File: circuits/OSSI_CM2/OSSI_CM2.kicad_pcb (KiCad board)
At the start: 4 copper layers, 49.5 x 54.9 mm, 76 parts, among them U101 STM32L412C8T6, U103 LM75B, U104 OPA2317, X101 PINHEADER_2×5, X201 Conn_01x20_Pin, X202 Conn_01x21_Pin, Y101 10MHz

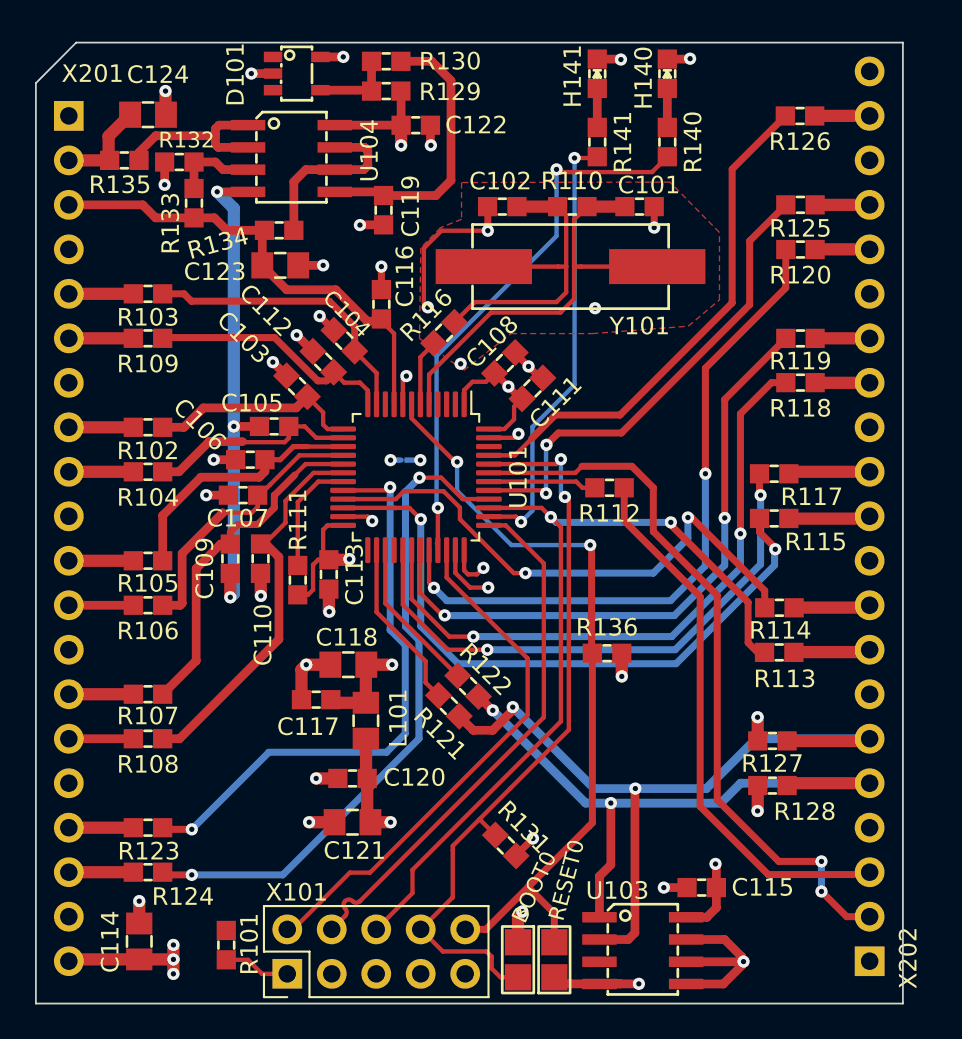
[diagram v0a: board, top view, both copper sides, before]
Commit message: Updates footprint paths
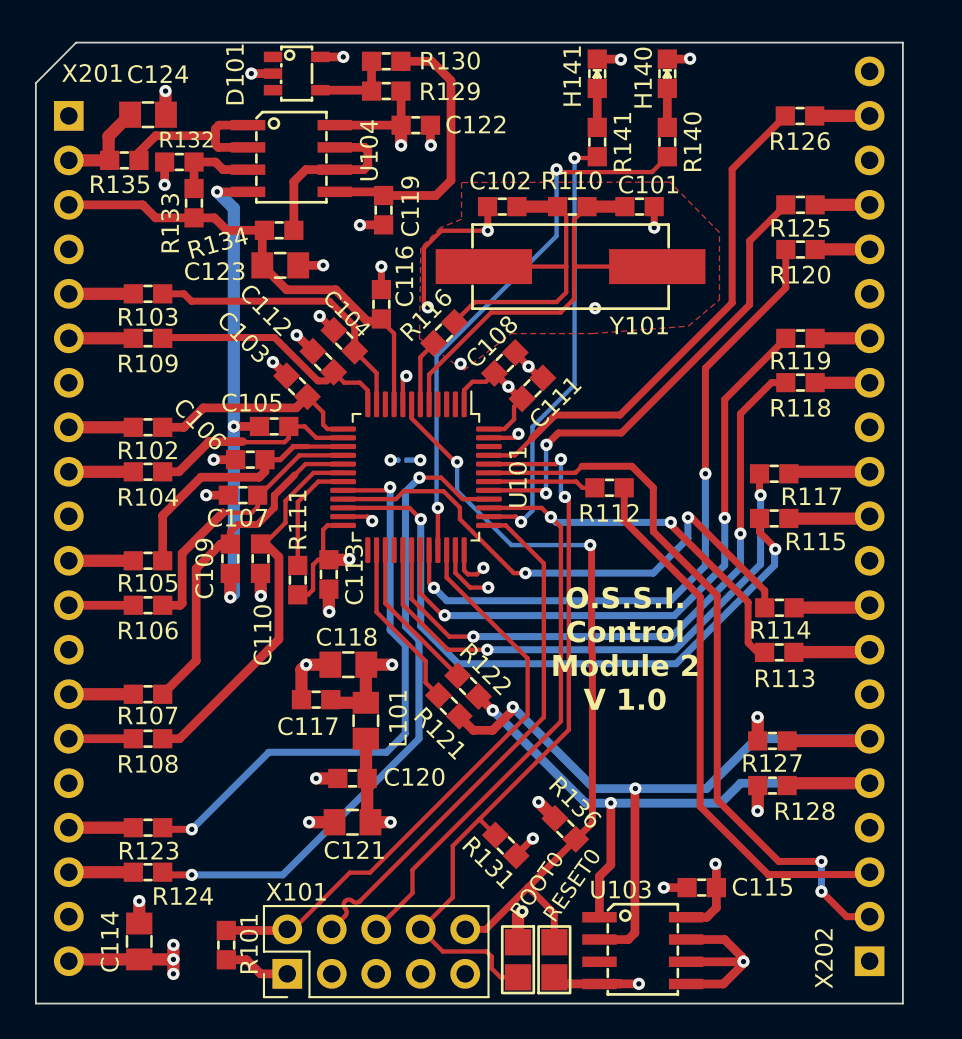
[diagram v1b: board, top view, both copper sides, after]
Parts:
- moved R136 10.3 mm to (147.7, 118.2), turned to -45 degrees
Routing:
- net Net-(U101C-PA3/ADC12_In8): track 15.3 -> 12.2 mm
- net /SWD_DIO/PA13: track 30.7 -> 33.3 mm
- net GND: track 47.7 -> 46.9 mm
- net +3V3: track 46.5 -> 45.7 mm
- net Net-(U101C-PB0/ADC12_In15): track 22.2 -> 21.7 mm
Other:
- board text added: "O.S.S.I. Control Module 2 V 1.0"
